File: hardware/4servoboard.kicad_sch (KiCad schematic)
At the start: 33 parts, among them J1 USB_C_Receptacle, J2 PWM, J3 UART, J4 GND, J5 V_SERVO, J6 POWER, J7 DEBUG, U1 CH32X035F7P6, U2 XC6206P332MR

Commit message: wip: Rev0.4への更新
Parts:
- removed D1: SERVO_PWR, LED_SMD:LED_0603_1608Metric_Pad1.05x0.95mm_HandSolder, symbol Device:LED
- removed J6: POWER, Connector_PinHeader_2.54mm:PinHeader_1x04_P2.54mm_Vertical, symbol Connector:Conn_01x04_Pin
- removed R10: 120k, Resistor_SMD:R_0603_1608Metric_Pad0.98x0.95mm_HandSolder, symbol PCM_SL_Resistors:Resistor
- removed R11: 5.1k, Resistor_SMD:R_0603_1608Metric_Pad0.98x0.95mm_HandSolder, symbol PCM_SL_Resistors:Resistor
- removed R5: 1k, Resistor_SMD:R_0603_1608Metric_Pad0.98x0.95mm_HandSolder, symbol PCM_SL_Resistors:Resistor
- added D3: MCU_LED2, LED_SMD:LED_0603_1608Metric_Pad1.05x0.95mm_HandSolder, symbol Device:LED
- added J6: VBUS, Connector_PinHeader_2.54mm:PinHeader_1x02_P2.54mm_Vertical, symbol Connector:Conn_01x02_Pin
- added J7: GND, Connector_PinHeader_2.54mm:PinHeader_1x02_P2.54mm_Vertical, symbol Connector:Conn_01x02_Pin
- added R6: 1k, Resistor_SMD:R_0603_1608Metric_Pad0.98x0.95mm_HandSolder, symbol PCM_SL_Resistors:Resistor
- added R9: 5k1, Resistor_SMD:R_0603_1608Metric_Pad0.98x0.95mm_HandSolder, symbol PCM_SL_Resistors:Resistor
- D2: value MCU_LED -> MCU_LED1
- J1: footprint PCM_SparkFun-Connector:USB-C_16 -> Download_Lib:USB-C_16-HandSolder
- J8: renamed from J7; footprint Connector_PinHeader_1.27mm:PinHeader_1x02_P1.27mm_Vertical -> Connector_PinHeader_2.54mm:PinHeader_1x02_P2.54mm_Vertical
- R10: renamed from R14; value 5.1k -> 5k1
- R11: renamed from R15; value 1k -> 22
- R12: renamed from R16; value 1k -> 22
- R13: renamed from R12; value 1k -> 5k1
- R14: renamed from R13; value 1k -> 5k1
- R8: value 5.1k -> 5k1
- TH1: value Thermistor_NTC -> 22k/B4050/NTC; footprint Resistor_SMD:R_0603_1608Metric_Pad0.98x0.95mm_HandSolder -> PCM_Resistor_SMD_AKL:R_0603_1608Metric_Pad0.98x0.95mm_HandSolder
- U2: footprint Package_TO_SOT_SMD:SOT-23_Handsoldering -> Package_TO_SOT_SMD:SOT-23
- renumbered R9 to R15, R6 to R5
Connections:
- net DP: now also R9.2; no longer JP1.1 (A)
- net GND: now also J7.1 (Pin_1), J7.2 (Pin_2)
- net VBUS: now also J6.1 (Pin_1), J6.2 (Pin_2)
- net VDD: now also R6.1
- net MCU_LED renamed MCU_LED1
- net MCU_LED1: now also U1.1 (PB12); no longer U1.12 (PA6)
- net OPA_N renamed PWM1/ADC1
- net PWM1/ADC1: now also J2.2 (Pin_2)
- net OPA_O: no longer names the net of U1.10 (PA4)
- net PB1 renamed V_SENCE
- net V_SENCE: now also U1.12 (PA6); no longer U1.14 (PB1)
- net PC3 renamed TEMP_SENCE
- net TEMP_SENCE: now also U1.14 (PB1); no longer U1.4 (RST/PC3)
- net PWM0 renamed PWM0/ADC0
- net PWM0/ADC0: now also U1.9 (PA3); no longer U1.1 (PB12)
- net PWM1 renamed PWM3/ADC3
- net PWM3/ADC3: now also J2.4 (Pin_4); no longer J2.2 (Pin_2)
- net PWM2 renamed PWM2/ADC2
- removed net PWM3: J2.4 (Pin_4), U1.9 (PA3)
- net TX2 renamed UART_A
- net UART_A: now also R12.2; no longer R11.2
- net TX4 renamed UART_B
- net UART_B: now also R11.2; no longer R12.2
- new net: JP1.1 (A), R9.1
- new net: D3.1 (K), R6.2
- new net MCU_LED2: D3.2 (A), U1.4 (RST/PC3)
- no-connect marks 0 -> 1
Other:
- moved on the sheet: C1, C2, C3, C4, D2, R5, U2

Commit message: fix: typo修正
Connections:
- net TEMP_SENCE renamed TEMP_SENSE
- net V_SENCE renamed V_SENSE
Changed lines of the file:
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@@
 		)
 	)
-	(global_label "TEMP_SENCE"
+	(global_label "TEMP_SENSE"
 		(shape input)
 		(at 210.82 97.79 180)
@@
 		)
 		(property "Intersheetrefs" "${INTERSHEET_REFS}"
-			(at 195.9212 97.79 0)
+			(at 195.9817 97.79 0)
 			(effects
 				(font
@@
 		)
 	)
-	(global_label "V_SENCE"
+	(global_label "V_SENSE"
 		(shape input)
 		(at 160.02 99.06 180)
@@
 		)
 		(property "Intersheetrefs" "${INTERSHEET_REFS}"
-			(at 148.8706 99.06 0)
+			(at 148.9311 99.06 0)
 			(effects
 				(font
@@
 		)
 	)
-	(global_label "TEMP_SENCE"
+	(global_label "TEMP_SENSE"
 		(shape input)
 		(at 48.26 121.92 180)
@@
 		)
 		(property "Intersheetrefs" "${INTERSHEET_REFS}"
-			(at 33.3612 121.92 0)
+			(at 33.4217 121.92 0)
 			(effects
 				(font
@@
 		)
 	)
-	(global_label "V_SENCE"
+	(global_label "V_SENSE"
 		(shape input)
 		(at 48.26 114.3 180)
@@
 		)
 		(property "Intersheetrefs" "${INTERSHEET_REFS}"
-			(at 37.1106 114.3 0)
-			(effects
-				(font
+			(at 37.1711 114.3 0)
+			(effects
+				(font

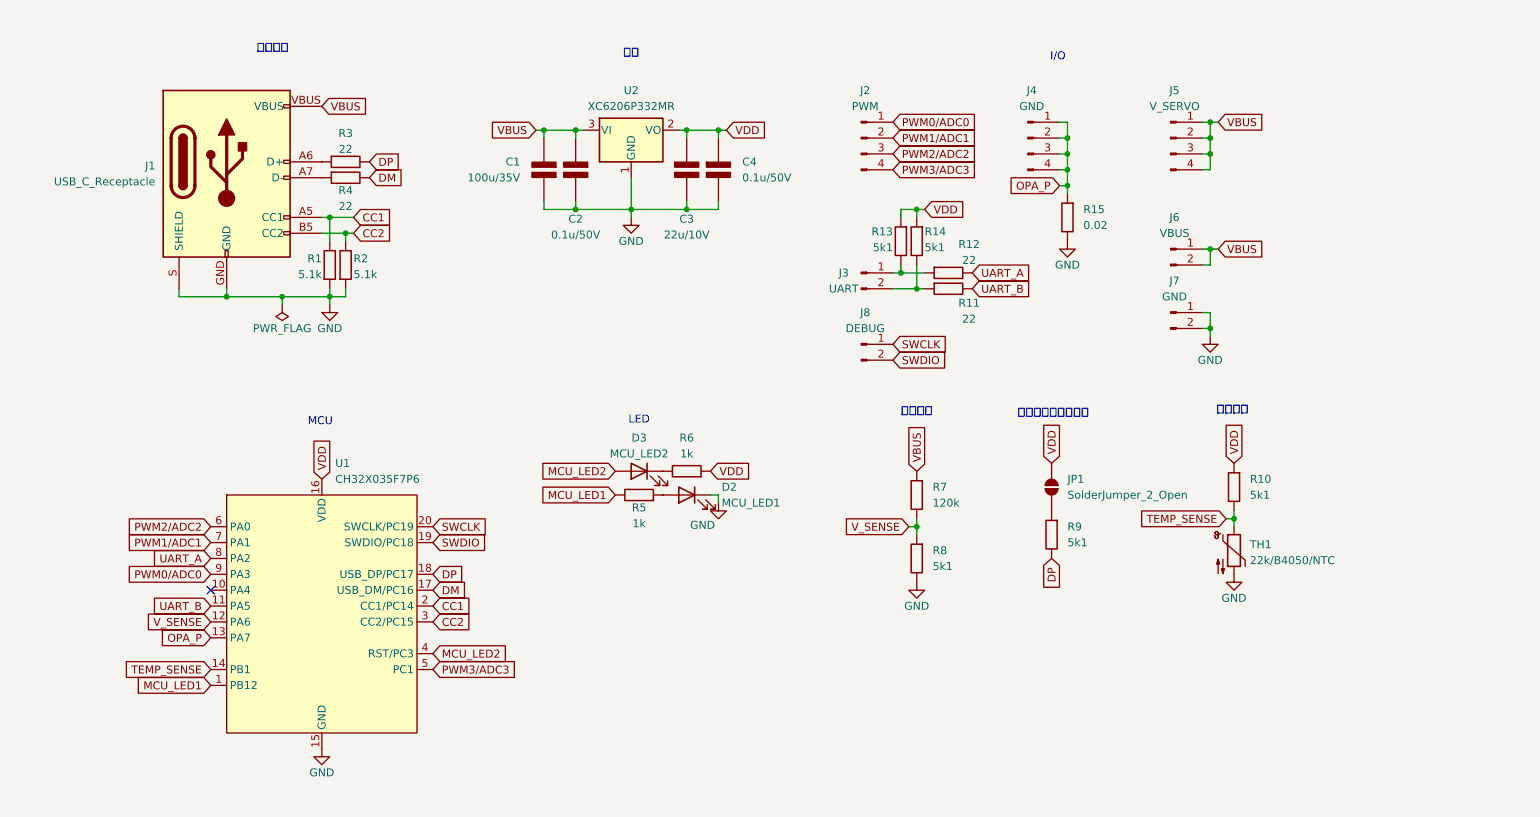
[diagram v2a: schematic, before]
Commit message: Update: V0.6移行に伴い，四層基板ヘ移行．エラッタ修正，Pch逆接保護回路追加，5.08端子追加
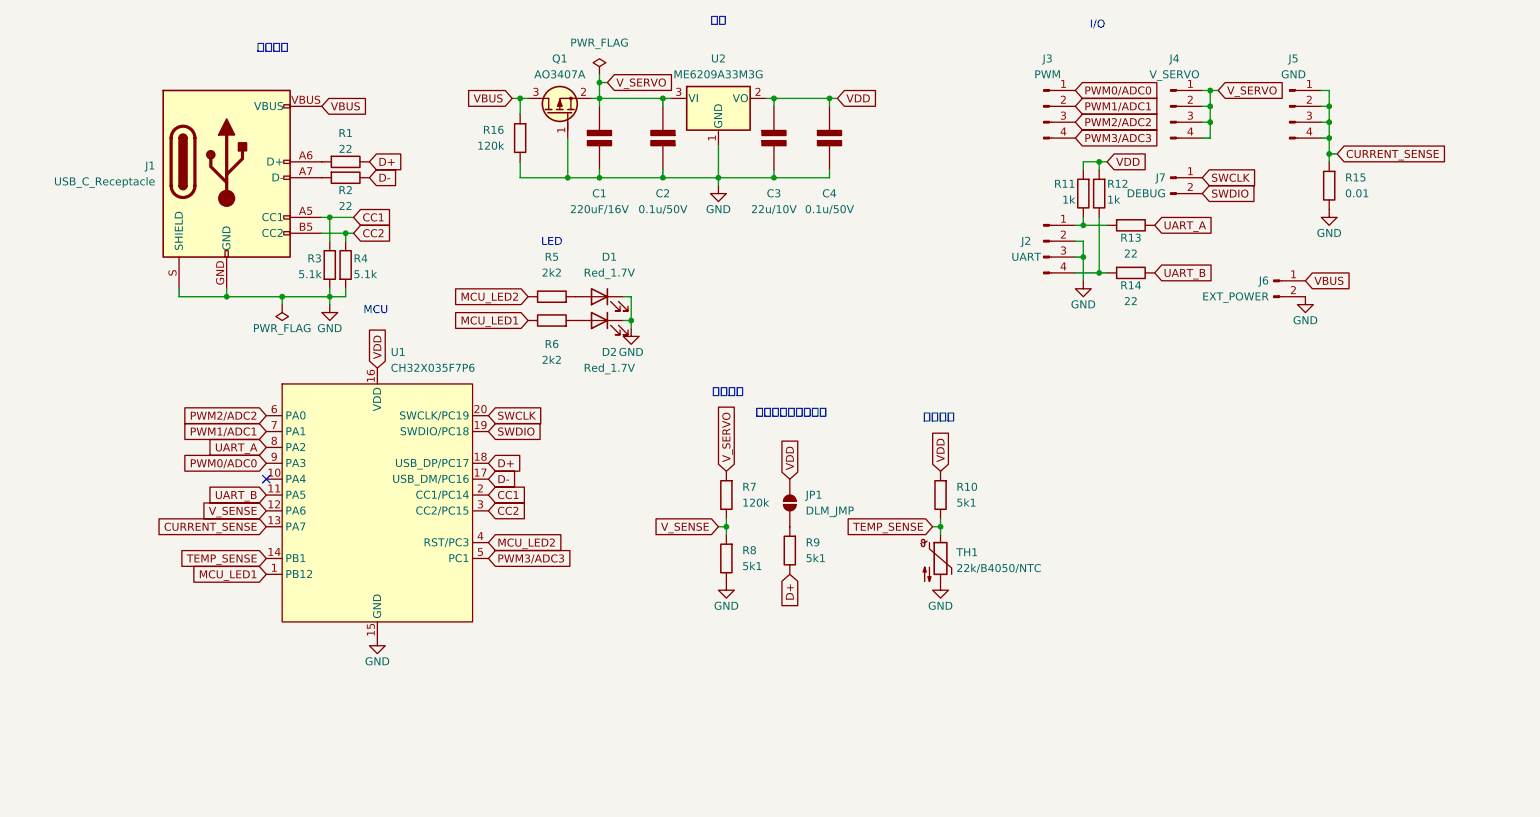
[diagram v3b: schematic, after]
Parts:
- removed J7: GND, Connector_PinHeader_2.54mm:PinHeader_1x02_P2.54mm_Vertical, symbol Connector:Conn_01x02_Pin
- added Q1: AO3407A, Package_TO_SOT_SMD:SOT-23, symbol PCM_Transistor_MOSFET_AKL:AO3407A
- added R16: 120k, Resistor_SMD:R_0603_1608Metric, symbol PCM_SL_Resistors:Resistor
- C1: value 100u/35V -> 220uF/16V
- C2, C3, C4: footprint Capacitor_SMD:C_0603_1608Metric_Pad1.08x0.95mm_HandSolder -> Capacitor_SMD:C_0603_1608Metric
- D1: renamed from D3; value MCU_LED2 -> Red_1.7V; footprint LED_SMD:LED_0603_1608Metric_Pad1.05x0.95mm_HandSolder -> LED_SMD:LED_0603_1608Metric
- D2: value MCU_LED1 -> Red_1.7V; footprint LED_SMD:LED_0603_1608Metric_Pad1.05x0.95mm_HandSolder -> LED_SMD:LED_0603_1608Metric
- J2: renamed from J3; footprint Connector_PinHeader_2.54mm:PinHeader_1x02_P2.54mm_Vertical -> Connector_PinHeader_2.54mm:PinHeader_1x04_P2.54mm_Vertical; symbol Connector:Conn_01x02_Pin -> Connector:Conn_01x04_Pin
- J6: value VBUS -> EXT_POWER; footprint Connector_PinHeader_2.54mm:PinHeader_1x02_P2.54mm_Vertical -> TerminalBlock:TerminalBlock_bornier-2_P5.08mm
- JP1: value SolderJumper_2_Open -> DLM_JMP; footprint Jumper:SolderJumper-2_P1.3mm_Open_RoundedPad1.0x1.5mm -> Jumper:SolderJumper-2_P1.3mm_Open_Pad1.0x1.5mm
- R1: renamed from R3; footprint Resistor_SMD:R_0603_1608Metric_Pad0.98x0.95mm_HandSolder -> Resistor_SMD:R_0603_1608Metric
- R10, R7, R8, R9: footprint Resistor_SMD:R_0603_1608Metric_Pad0.98x0.95mm_HandSolder -> Resistor_SMD:R_0603_1608Metric
- R11: renamed from R13; value 5k1 -> 1k; footprint Resistor_SMD:R_0603_1608Metric_Pad0.98x0.95mm_HandSolder -> Resistor_SMD:R_0603_1608Metric
- R12: renamed from R14; value 5k1 -> 1k; footprint Resistor_SMD:R_0603_1608Metric_Pad0.98x0.95mm_HandSolder -> Resistor_SMD:R_0603_1608Metric
- R13: renamed from R12; footprint Resistor_SMD:R_0603_1608Metric_Pad0.98x0.95mm_HandSolder -> Resistor_SMD:R_0603_1608Metric
- R14: renamed from R11; footprint Resistor_SMD:R_0603_1608Metric_Pad0.98x0.95mm_HandSolder -> Resistor_SMD:R_0603_1608Metric
- R15: value 0.02 -> 0.01; footprint Resistor_SMD:R_1206_3216Metric_Pad1.30x1.75mm_HandSolder -> Resistor_SMD:R_1206_3216Metric
- R2: renamed from R4; footprint Resistor_SMD:R_0603_1608Metric_Pad0.98x0.95mm_HandSolder -> Resistor_SMD:R_0603_1608Metric
- R3: renamed from R1; footprint Resistor_SMD:R_0603_1608Metric_Pad0.98x0.95mm_HandSolder -> Resistor_SMD:R_0603_1608Metric
- R4: renamed from R2; footprint Resistor_SMD:R_0603_1608Metric_Pad0.98x0.95mm_HandSolder -> Resistor_SMD:R_0603_1608Metric
- R5, R6: value 1k -> 2k2; footprint Resistor_SMD:R_0603_1608Metric_Pad0.98x0.95mm_HandSolder -> Resistor_SMD:R_0603_1608Metric
- TH1: footprint PCM_Resistor_SMD_AKL:R_0603_1608Metric_Pad0.98x0.95mm_HandSolder -> Resistor_SMD:R_0603_1608Metric
- U2: value XC6206P332MR -> ME6209A33M3G
- renumbered J2 to J3, J5 to J4, J4 to J5, J8 to J7
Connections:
- net GND: now also C1.2 (-), D1.1 (K), J2.2 (Pin_2), J2.3 (Pin_3), J6.2 (Pin_2), Q1.1 (G), R16.2; no longer C1.1 (+)
- net MCU_LED1: now also R6.2; no longer R5.2
- net MCU_LED2: now also R5.2; no longer D1.2 (A)
- net VBUS: now also Q1.3 (D), R16.1; no longer C1.2 (-), C2.2 (-), J4.1 (Pin_1), J4.2 (Pin_2), J4.3 (Pin_3), J4.4 (Pin_4), J6.2 (Pin_2), R7.1, U2.3 (VI)
- net VDD: no longer R6.1
- net at R5.1: now also D1.2 (A); no longer D2.2 (A)
- net at R12.2, R14.1: now also J2.4 (Pin_4); no longer J2.2 (Pin_2)
- net DM renamed D-
- net DP renamed D+
- net OPA_P renamed CURRENT_SENSE
- new net: D2.2 (A), R6.1
- new net V_SERVO: C1.1 (+), C2.2 (-), J4.1 (Pin_1), J4.2 (Pin_2), J4.3 (Pin_3), J4.4 (Pin_4), Q1.2 (S), R7.1, U2.3 (VI)
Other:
- note added: "温度計測"
- note removed: "温度監視"
- moved on the sheet: C1, C2, C3, C4, D1, D2, J3, J4, J5, J6, J7, JP1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

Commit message: Fix: 基板デザインの効率化が主．内容：アートワークの最適化，viaの追加など
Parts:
- R5, R6: value 2k2 -> 1k
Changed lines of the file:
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@@
 			)
 		)
-		(property "Value" "2k2"
+		(property "Value" "1k"
 			(at 102.87 58.42 0)
 			(effects
@@
 			)
 		)
-		(property "Value" "2k2"
+		(property "Value" "1k"
 			(at 102.87 72.39 0)
 			(effects

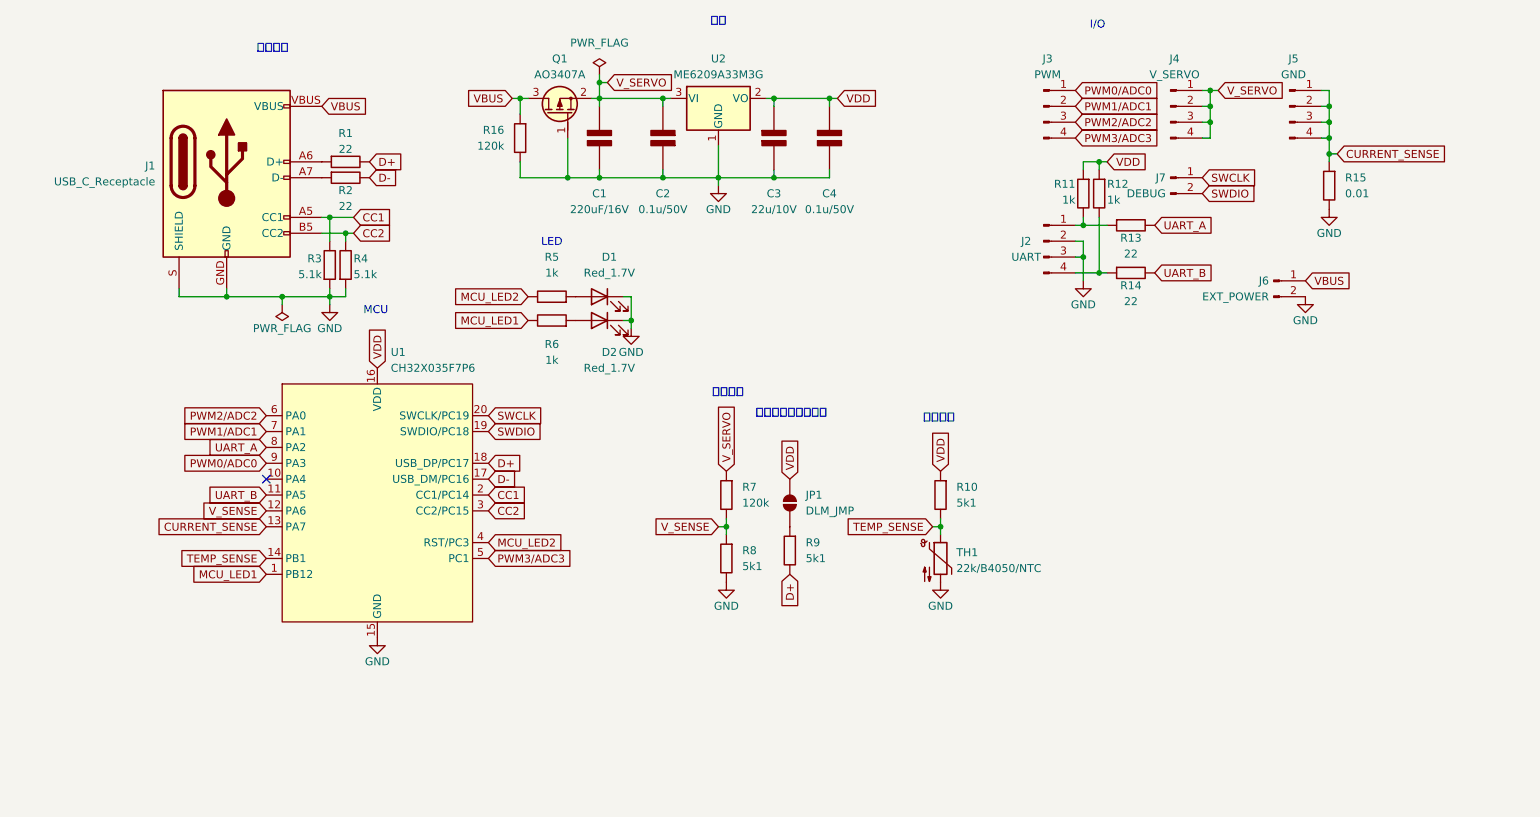
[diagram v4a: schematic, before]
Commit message: Update: V0.7移行．ORing回路実装，電源設計の効率化，回路定数の見直し
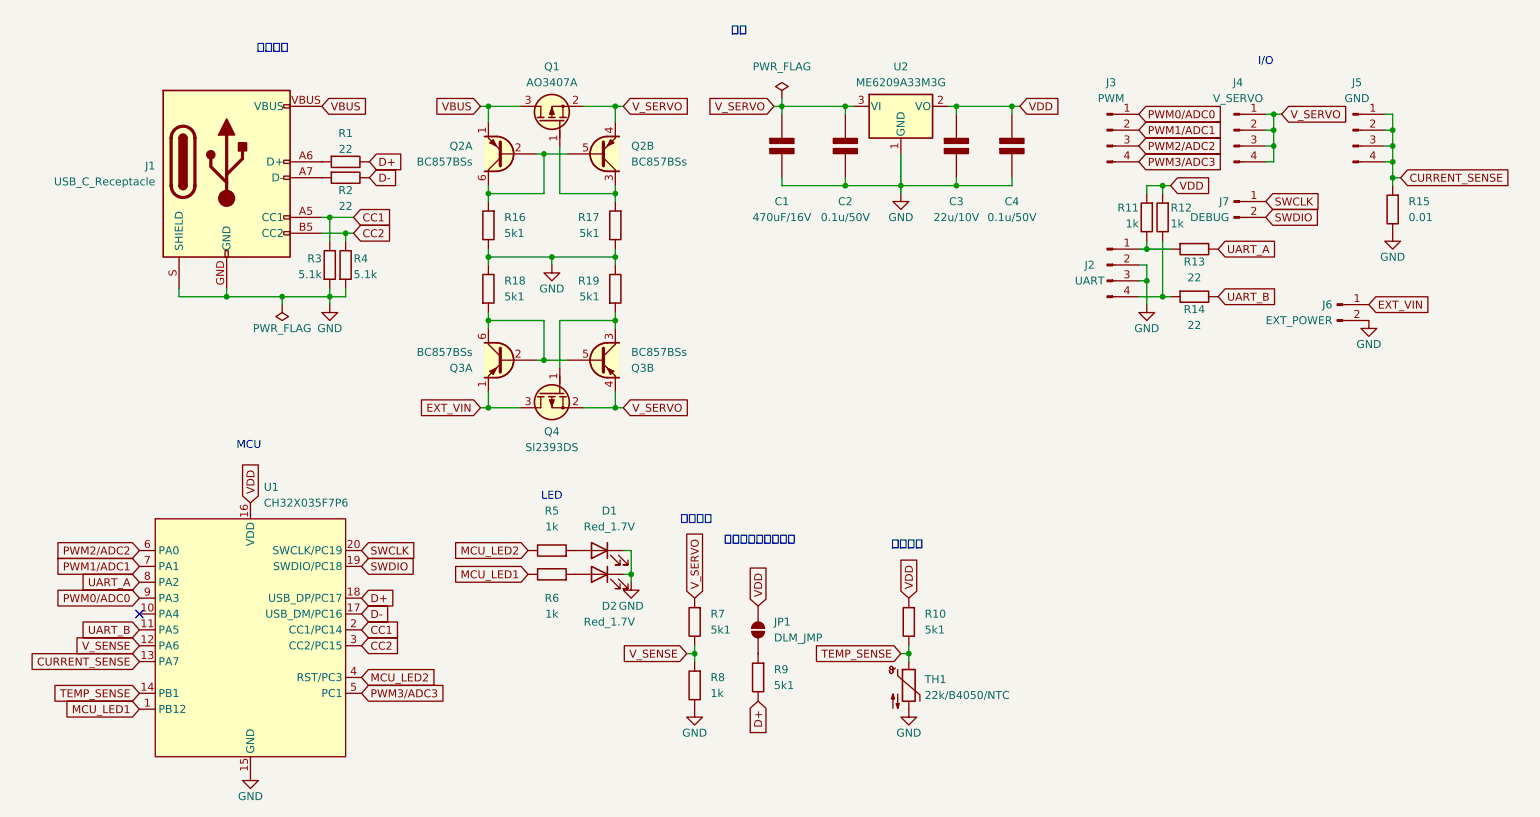
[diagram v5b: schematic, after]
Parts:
- added Q2, Q3: BC857BSs, PCM_Package_TO_SOT_SMD_AKL:SOT-363_SC-70-6, symbol PCM_Transistor_BJT_AKL:BC857BSs
- added Q4: SI2393DS, Package_TO_SOT_SMD:SOT-23, symbol PCM_Transistor_MOSFET_AKL:AO3407A
- added R17, R18, R19: 5k1, Resistor_SMD:R_0603_1608Metric, symbol PCM_SL_Resistors:Resistor
- C1: value 220uF/16V -> 470uF/16V
- J6: footprint TerminalBlock:TerminalBlock_bornier-2_P5.08mm -> TerminalBlock:TerminalBlock_Xinya_XY308-2.54-2P_1x02_P2.54mm_Horizontal
- R16, R7: value 120k -> 5k1
- R8: value 5k1 -> 1k
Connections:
- net GND: now also R17.2, R18.2, R19.2; no longer Q1.1 (G)
- net VBUS: now also Q2.1 (E1); no longer J6.1 (Pin_1), R16.1
- net V_SERVO: now also Q2.4 (E2), Q3.4 (E2), Q4.2 (S)
- new net: Q3.3 (C2), Q4.1 (G), R19.1
- new net: Q3.2 (B1), Q3.5 (B2), Q3.6 (C1), R18.1
- new net: Q1.1 (G), Q2.3 (C2), R17.1
- new net: Q2.2 (B1), Q2.5 (B2), Q2.6 (C1), R16.1
- new net EXT_VIN: J6.1 (Pin_1), Q3.1 (E1), Q4.3 (D)
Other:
- moved on the sheet: C1, C2, C3, C4, D1, D2, J2, J3, J4, J5, J6, J7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

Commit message: Update: V0.8移行．回路設計の効率化．エラッタの修正
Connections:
- net GND: no longer D1.1 (K)
- net MCU_LED2: now also D1.2 (A); no longer R5.2
- net VDD: now also R5.1
- new net: D1.1 (K), R5.2
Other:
- moved on the sheet: D1, R5
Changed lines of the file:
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@@
 	(title_block
 		(title "UART-FourServoControllBoard")
-		(date "2026-02-08")
-		(rev "V0.7")
+		(date "2026-02-11")
+		(rev "V0.8")
 		(company "EsEhEhElp")
 	)
@@
 	)
 	(junction
-		(at 115.57 106.68)
-		(diameter 0)
-		(color 0 0 0 0)
-	)
-	(junction
 		(at 59.69 62.23)
 		(diameter 0)
@@
 	(wire
 		(pts
-			(xy 115.57 102.87) (xy 115.57 106.68)
-		)
-		(stroke
-			(width 0)
-			(type default)
-		)
-	)
-	(wire
-		(pts
 			(xy 104.14 45.72) (xy 113.03 45.72)
 		)
@@
 	(wire
 		(pts
-			(xy 114.3 102.87) (xy 115.57 102.87)
-		)
-		(stroke
-			(width 0)
-			(type default)
-		)
-	)
-	(wire
-		(pts
 			(xy 218.44 38.1) (xy 218.44 40.64)
 		)
@@
 		)
 	)
+	(global_label "VDD"
+		(shape input)
+		(at 114.3 102.87 0)
+		(fields_autoplaced yes)
+		(effects
+			(font
+				(size 1.27 1.27)
+			)
+			(justify left)
+		)
+		(property "Intersheetrefs" "${INTERSHEET_REFS}"
+			(at 120.9138 102.87 0)
+			(effects
+				(font
+					(size 1.27 1.27)
+				)
+				(justify left)
+				(hide yes)
+			)
+		)
+	)
 	(global_label "SWDIO"
 		(shape input)
@@
 	(symbol
 		(lib_id "PCM_SL_Resistors:Resistor")
-		(at 102.87 102.87 180)
+		(at 110.49 102.87 180)
 		(unit 1)
 		(exclude_from_sim no)
@@
 		(fields_autoplaced yes)
 		(property "Reference" "R5"
-			(at 102.87 96.52 0)
+			(at 110.49 96.52 0)
 			(effects
 				(font
@@
 		)
 		(property "Value" "1k"
-			(at 102.87 99.06 0)
+			(at 110.49 99.06 0)
 			(effects
 				(font
@@
 		)
 		(property "Footprint" "Resistor_SMD:R_0603_1608Metric"
-			(at 101.981 98.552 0)
+			(at 109.601 98.552 0)
 			(effects
 				(font
@@
 		)
 		(property "Datasheet" ""
-			(at 102.362 102.87 0)
+			(at 109.982 102.87 0)
 			(effects
 				(font
@@
 		)
 		(property "Description" "1/4W Resistor"
-			(at 102.87 102.87 0)
+			(at 110.49 102.87 0)
 			(effects
 				(font
@@
 	(symbol
 		(lib_id "Device:LED")
-		(at 110.49 102.87 0)
+		(at 102.87 102.87 0)
 		(mirror y)
 		(unit 1)
@@
 		(fields_autoplaced yes)
 		(property "Reference" "D1"
-			(at 112.0775 96.52 0)
+			(at 104.4575 96.52 0)
 			(effects
 				(font
@@
 		)
 		(property "Value" "Red_1.7V"
-			(at 112.0775 99.06 0)
+			(at 104.4575 99.06 0)
 			(effects
 				(font
@@
 		)
 		(property "Footprint" "LED_SMD:LED_0603_1608Metric"
-			(at 110.49 102.87 0)
+			(at 102.87 102.87 0)
 			(effects
 				(font
@@
 		)
 		(property "Datasheet" "~"
-			(at 110.49 102.87 0)
+			(at 102.87 102.87 0)
 			(effects
 				(font
@@
 		)
 		(property "Description" "Light emitting diode"
-			(at 110.49 102.87 0)
+			(at 102.87 102.87 0)
 			(effects
 				(font
@@
 		)
 		(property "Sim.Pins" "1=K 2=A"
-			(at 110.49 102.87 0)
+			(at 102.87 102.87 0)
 			(effects
 				(font
